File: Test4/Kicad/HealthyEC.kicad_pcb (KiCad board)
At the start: 2 copper layers, 29.3 x 33 mm, 28 parts, among them P1 CONN_5, U1 MCP6244, U2 MCP6241

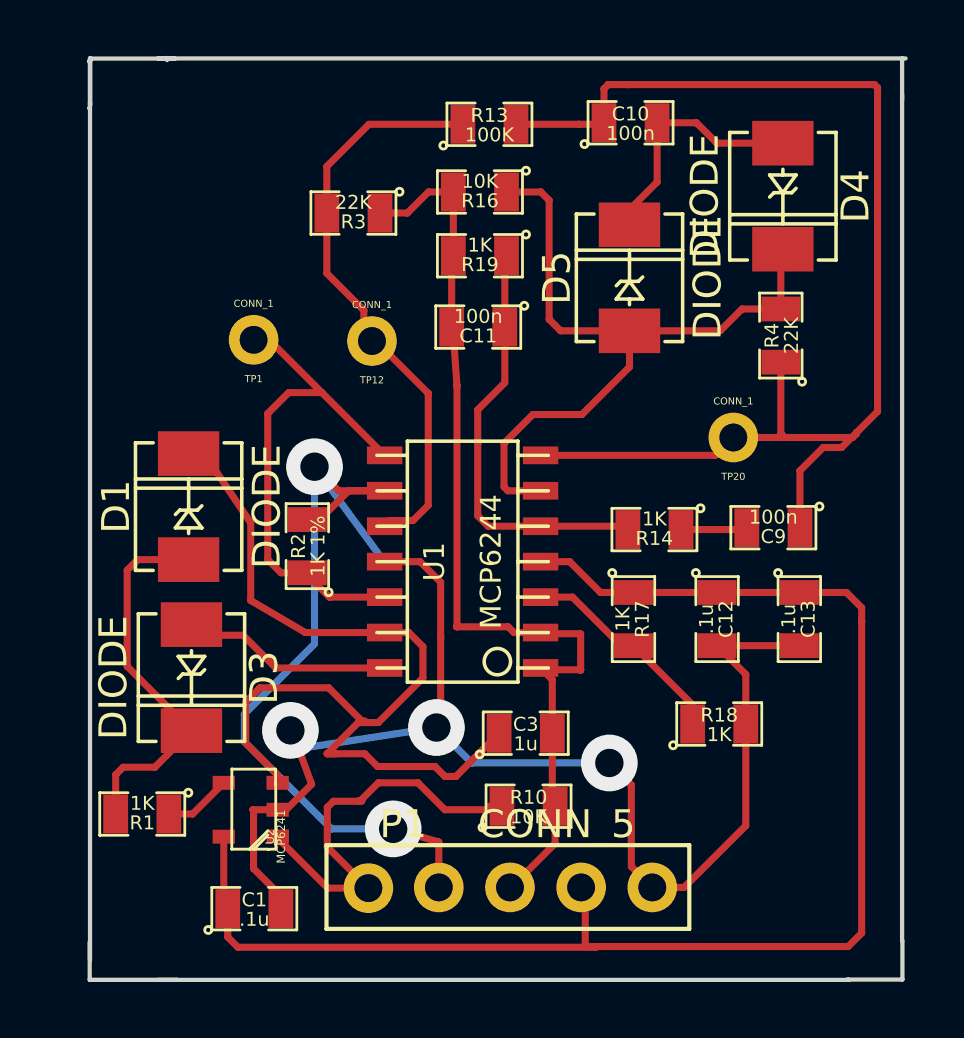
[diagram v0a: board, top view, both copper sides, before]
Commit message: fixed mistake in schematic/layout for AD to DC conversion
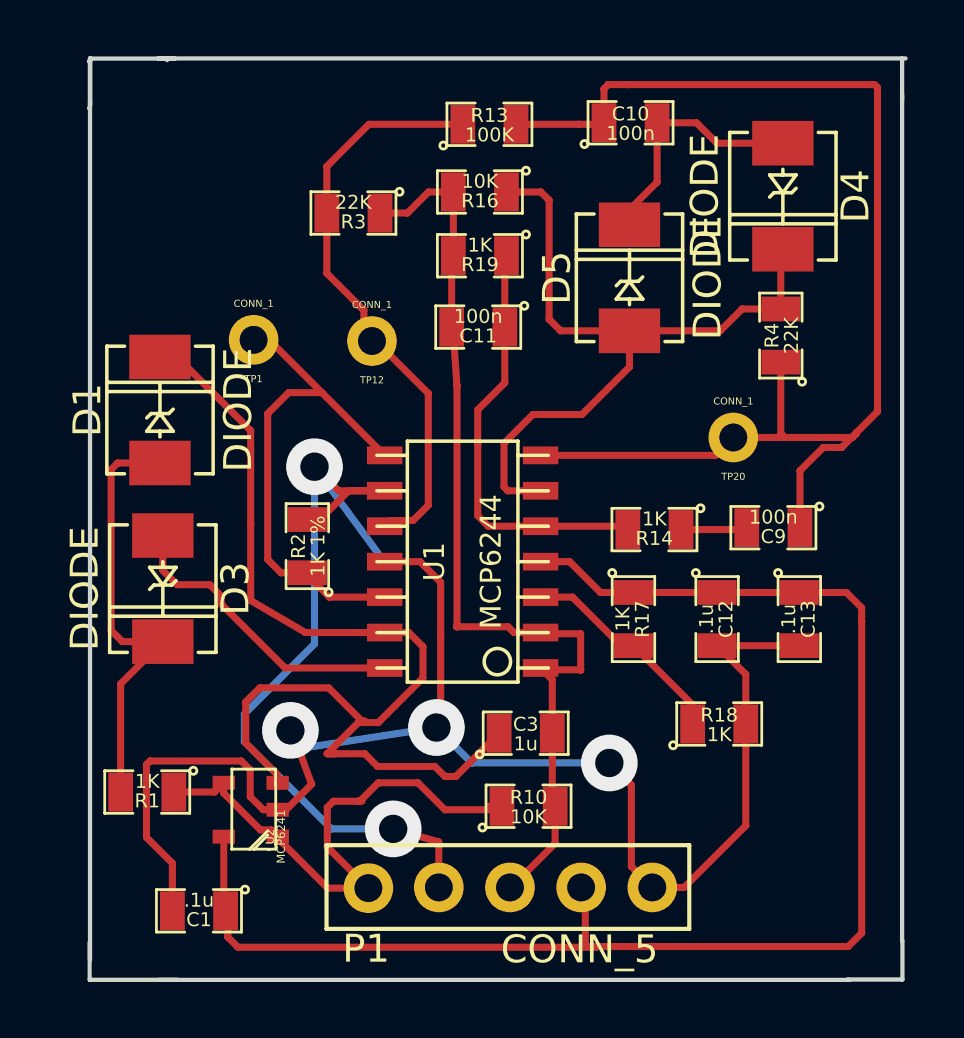
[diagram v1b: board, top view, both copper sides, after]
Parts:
- moved D1 3.61 mm to (28.8, 27.1)
- moved D3 3.35 mm to (28.9, 33.5)
- moved C1 1.99 mm to (30.2, 45.0), turned to 180 degrees
- moved R1 0.81 mm to (28.3, 40.8)
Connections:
- net /EC/pin 13 renamed /EC/pin 13&3
- R1 pad 1: /EC/pin 1 -> /EC/EC_Meas
- U2 pad 4: /EC/pin 1 -> /EC/EC_Meas
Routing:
- net AGND: track 48.2 -> 55.0 mm
- net /EC/EC_Meas: track 15.3 -> 20.1 mm
- net /EC/pin 13&3: track 34.6 -> 38.7 mm
- net /EC/pin 14: track 7.57 -> 11.5 mm
- net /EC/pin 1: track 2.43 -> 0.00 mm
- net /EC/DD: track 13.8 -> 15.6 mm

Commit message: fixed track to nowhere on back layer
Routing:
- net /EC/EC_Probe+: track 31.2 -> 27.2 mm
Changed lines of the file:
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@@
     (thickness 1.6)
     (drawings 19)
-    (tracks 267)
+    (tracks 266)
     (zones 0)
     (modules 28)
@@
     (visible_elements 7FFFFFFF)
     (pcbplotparams
-      (layerselection 3178497)
+      (layerselection 271613953)
       (usegerberextensions true)
       (excludeedgelayer true)
@@
   (gr_line (start 55.3847 47.4853) (end 53.4162 47.4853) (angle 90) (layer Edge.Cuts) (width 0.1524))
   (gr_line (start 55.3847 46.101) (end 55.3847 47.4853) (angle 90) (layer Edge.Cuts) (width 0.1524))
-  (segment (start 28.7782 28.97632) (end 27.26182 28.97632) (width 0.254) (layer F.Cu) (net 1) (status 400000))
-  (segment (start 27.42946 35.37712) (end 28.8798 35.37712) (width 0.254) (layer F.Cu) (net 1) (status 800000))
+  (segment (start 28.7782 28.97632) (end 27.26182 28.97632) (width 0.254) (layer F.Cu) (net 1))
+  (segment (start 27.42946 35.37712) (end 28.8798 35.37712) (width 0.254) (layer F.Cu) (net 1))
   (segment (start 27.0256 34.97326) (end 27.42946 35.37712) (width 0.254) (layer F.Cu) (net 1))
   (segment (start 27.0256 29.21254) (end 27.0256 34.97326) (width 0.254) (layer F.Cu) (net 1))
   (segment (start 27.26182 28.97632) (end 27.0256 29.21254) (width 0.254) (layer F.Cu) (net 1))
-  (segment (start 27.3685 40.767) (end 27.3685 36.88842) (width 0.254) (layer F.Cu) (net 1) (status 400000))
-  (segment (start 27.3685 36.88842) (end 28.8798 35.37712) (width 0.254) (layer F.Cu) (net 1) (status 800000))
-  (segment (start 29.2735 40.767) (end 30.734 40.767) (width 0.254) (layer F.Cu) (net 2) (status 400000))
-  (segment (start 30.734 40.767) (end 31.0642 40.4368) (width 0.254) (layer F.Cu) (net 2) (status 800000))
-  (segment (start 31.0642 40.4368) (end 31.0642 40.81018) (width 0.254) (layer F.Cu) (net 2) (status 400000))
-  (segment (start 32.76346 42.12336) (end 32.99968 42.35958) (width 0.254) (layer F.Cu) (net 2) (status C00000))
-  (segment (start 32.37738 42.12336) (end 32.76346 42.12336) (width 0.254) (layer F.Cu) (net 2) (status 800000))
+  (segment (start 27.3685 40.767) (end 27.3685 36.88842) (width 0.254) (layer F.Cu) (net 1))
+  (segment (start 27.3685 36.88842) (end 28.8798 35.37712) (width 0.254) (layer F.Cu) (net 1))
+  (segment (start 29.2735 40.767) (end 30.734 40.767) (width 0.254) (layer F.Cu) (net 2))
+  (segment (start 30.734 40.767) (end 31.0642 40.4368) (width 0.254) (layer F.Cu) (net 2))
+  (segment (start 31.0642 40.4368) (end 31.0642 40.81018) (width 0.254) (layer F.Cu) (net 2))
+  (segment (start 32.76346 42.12336) (end 32.99968 42.35958) (width 0.254) (layer F.Cu) (net 2))
+  (segment (start 32.37738 42.12336) (end 32.76346 42.12336) (width 0.254) (layer F.Cu) (net 2))
   (segment (start 31.0642 40.81018) (end 32.37738 42.12336) (width 0.254) (layer F.Cu) (net 2))
   (segment (start 36.2458 44.2106) (end 34.7872 44.2106) (width 0.254) (layer F.Cu) (net 2))
@@
   (segment (start 34.3154 35.4584) (end 31.8008 37.973) (width 0.254) (layer B.Cu) (net 3))
   (segment (start 36.83 29.972) (end 35.179 29.972) (width 0.254) (layer F.Cu) (net 3))
-  (segment (start 34.3154 29.1084) (end 36.703 32.3596) (width 0.254) (layer B.Cu) (net 3))
   (via (at 34.3154 29.1084) (size 2.032) (layers F.Cu B.Cu) (net 3))
   (segment (start 35.179 29.972) (end 34.3154 29.1084) (width 0.254) (layer F.Cu) (net 3))
@@
   (segment (start 49.74082 31.36138) (end 49.80686 31.29534) (width 0.254) (layer F.Cu) (net 7))
   (segment (start 32.0294 31.1404) (end 32.0294 27.81554) (width 0.254) (layer F.Cu) (net 8))
-  (segment (start 29.39034 25.17648) (end 28.7782 25.17648) (width 0.254) (layer F.Cu) (net 8) (status C00000))
-  (segment (start 32.0294 27.81554) (end 29.39034 25.17648) (width 0.254) (layer F.Cu) (net 8) (status 800000))
+  (segment (start 29.39034 25.17648) (end 28.7782 25.17648) (width 0.254) (layer F.Cu) (net 8))
+  (segment (start 32.0294 27.81554) (end 29.39034 25.17648) (width 0.254) (layer F.Cu) (net 8))
   (segment (start 32.0294 31.12008) (end 32.0294 31.1404) (width 0.254) (layer F.Cu) (net 8))
   (segment (start 32.0294 31.1404) (end 32.0294 33.90392) (width 0.254) (layer F.Cu) (net 8))
@@
   (segment (start 33.99028 35.052) (end 36.83 35.052) (width 0.254) (layer F.Cu) (net 8))
   (segment (start 32.0294 33.90392) (end 33.99028 35.052) (width 0.254) (layer F.Cu) (net 8))
-  (segment (start 36.83 36.322) (end 33.26384 36.322) (width 0.254) (layer F.Cu) (net 9) (status 400000))
-  (segment (start 28.8798 32.82696) (end 28.8798 31.57728) (width 0.254) (layer F.Cu) (net 9) (status 800000))
+  (segment (start 36.83 36.322) (end 33.26384 36.322) (width 0.254) (layer F.Cu) (net 9))
+  (segment (start 28.8798 32.82696) (end 28.8798 31.57728) (width 0.254) (layer F.Cu) (net 9))
   (segment (start 29.39034 33.3375) (end 28.8798 32.82696) (width 0.254) (layer F.Cu) (net 9))
   (segment (start 30.56382 33.3375) (end 29.39034 33.3375) (width 0.254) (layer F.Cu) (net 9))
@@
   (segment (start 30.97276 34.03092) (end 30.97276 33.74644) (width 0.254) (layer F.Cu) (net 9))
   (segment (start 33.26384 36.322) (end 30.97276 34.03092) (width 0.254) (layer F.Cu) (net 9))
-  (segment (start 28.8798 31.57728) (end 28.8798 32.27324) (width 0.254) (layer F.Cu) (net 9) (status C00000))
+  (segment (start 28.8798 31.57728) (end 28.8798 32.27324) (width 0.254) (layer F.Cu) (net 9))
   (segment (start 47.8663 38.3286) (end 47.8663 37.6428) (width 0.254) (layer F.Cu) (net 10))
   (segment (start 47.8663 37.6428) (end 45.7454 35.5219) (width 0.254) (layer F.Cu) (net 10))
@@
   (segment (start 34.75736 18.34642) (end 34.75736 20.01774) (width 0.254) (layer F.Cu) (net 14))
   (segment (start 36.26612 16.83766) (end 34.75736 18.34642) (width 0.254) (layer F.Cu) (net 14))
-  (segment (start 29.2227 45.02404) (end 29.2227 43.3197) (width 0.254) (layer F.Cu) (net 15) (status 400000))
-  (segment (start 32.47898 41.402) (end 32.9946 41.402) (width 0.254) (layer F.Cu) (net 15) (status 800000))
+  (segment (start 29.2227 45.02404) (end 29.2227 43.3197) (width 0.254) (layer F.Cu) (net 15))
+  (segment (start 32.47898 41.402) (end 32.9946 41.402) (width 0.254) (layer F.Cu) (net 15))
   (segment (start 32.01162 40.93464) (end 32.47898 41.402) (width 0.254) (layer F.Cu) (net 15))
   (segment (start 32.01162 39.97452) (end 32.01162 40.93464) (width 0.254) (layer F.Cu) (net 15))
